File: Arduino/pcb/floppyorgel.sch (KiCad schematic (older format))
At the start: 25 parts, among them J1 Floppy-Bus, J2 Floppy-Bus, J3 FTDI, J4 Buck-Converter-5V, J5 MAX485 Socket, J6 Buck-Converter-12V, J7 IBM_PC_Floppy_IDC, J8 Power Select, J9 Floppy-Power, SW1 Bus Address Select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

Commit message: floppyorgel.sch: wiring shift registers
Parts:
- removed U3: 74LS166, SMD_Packages:SO-16-N, symbol floppyorgel-rescue:74LS166-74xx
- added R? (x4): 4K7, symbol Device:R
- added U?: 4021, symbol 4xxx_IEEE:4021
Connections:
- net labels added: DIRECTION, DRIVE_SELECT, STEP, TRK00, nLATCH
- wire segments 146 -> 162
- no-connect marks 15 -> 23
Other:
- moved on the sheet: C?, J7, R?, SW1, SW2, U1, Y1

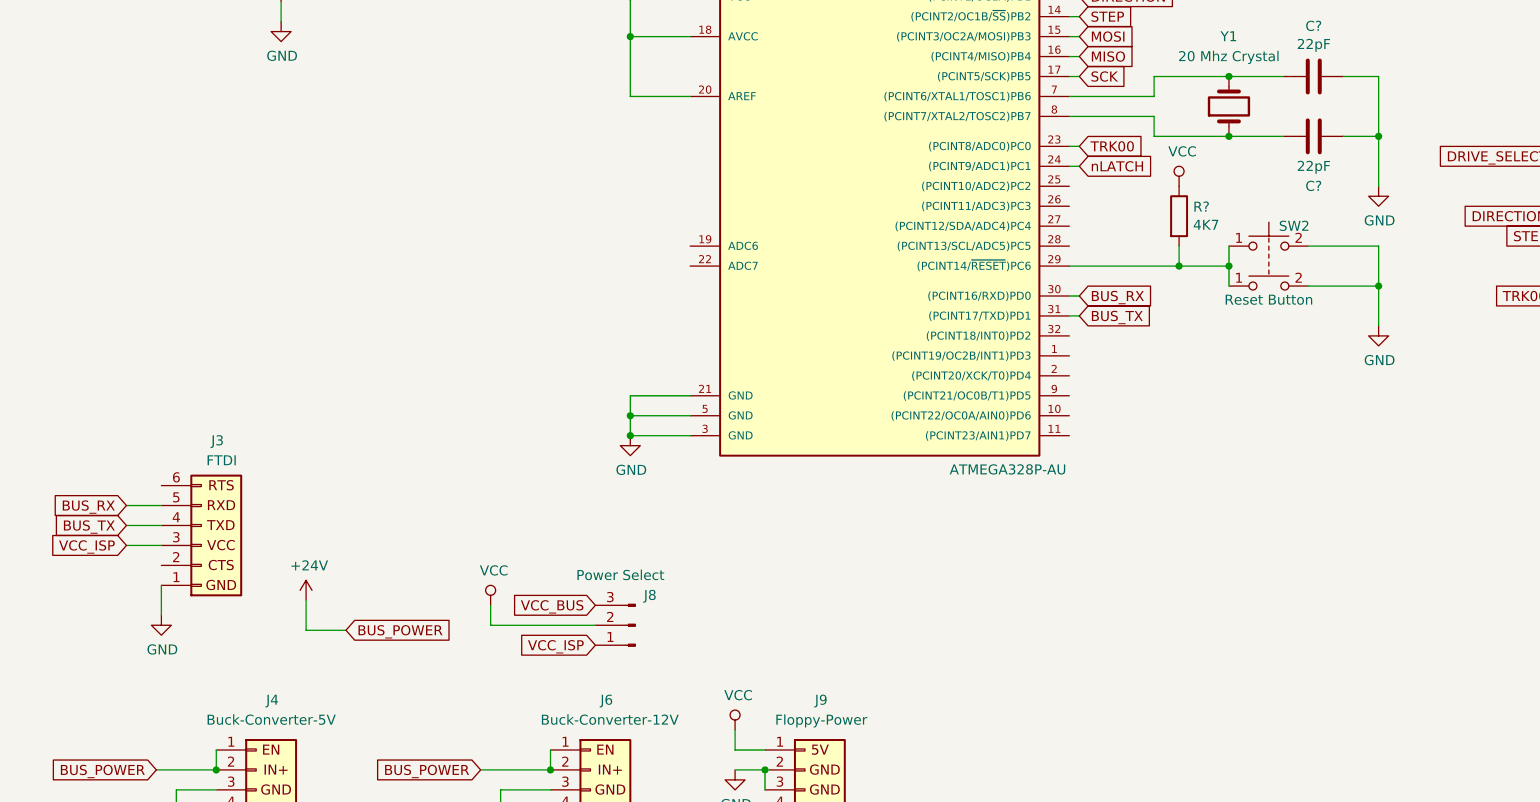
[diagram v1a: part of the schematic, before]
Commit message: floppyorgel.sch: wiring reset circuit
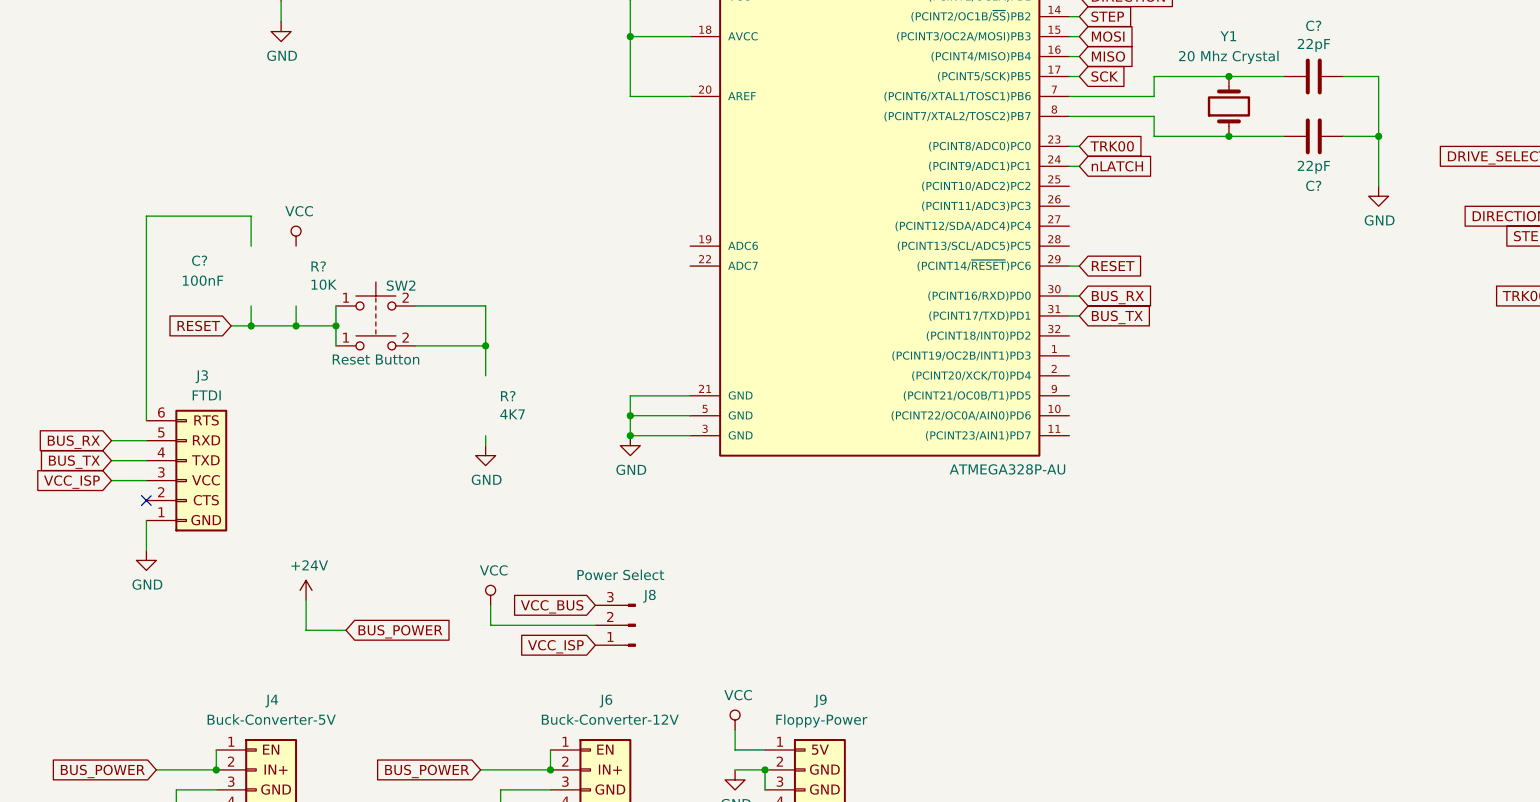
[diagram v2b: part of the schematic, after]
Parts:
- added C?: 100nF, symbol Device:C
- added R?: 4K7, symbol Device:R
- R?: value 4K7 -> 10K
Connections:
- net labels added: RESET
- wire segments 162 -> 169
- no-connect marks 23 -> 24
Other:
- moved on the sheet: J3, SW2
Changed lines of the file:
@@
 Sheet 1 1
 Title "Floppy Orgel"
-Date "2018-06-28"
+Date "2019-04-22"
 Rev "0"
 Comp "coon@c-base.org"
@@
 L floppyorgel-rescue:SW_Push_Dual-RESCUE-floppyorgel SW2
 U 1 1 5B36C9BB
-P 6825 4275
-F 0 "SW2" H 6875 4375 50  0000 L CNN
-F 1 "Reset Button" H 6825 4005 50  0000 C CNN
-F 2 "Buttons_Switches_THT:SW_PUSH_6mm" H 6825 4475 50  0001 C CNN
-F 3 "" H 6825 4475 50  0001 C CNN
-	1    6825 4275
+P 2350 4575
+F 0 "SW2" H 2400 4675 50  0000 L CNN
+F 1 "Reset Button" H 2350 4305 50  0000 C CNN
+F 2 "Buttons_Switches_THT:SW_PUSH_6mm" H 2350 4775 50  0001 C CNN
+F 3 "" H 2350 4775 50  0001 C CNN
+	1    2350 4575
 	1    0    0    -1
 $EndComp
@@
 L ftdi:FTDI J3
 U 1 1 5C74FB67
-P 1475 5775
-F 0 "J3" H 1525 5250 50  0000 L CNN
-F 1 "FTDI" H 1500 5350 50  0000 L CNN
-F 2 "Connector_PinHeader_2.54mm:PinHeader_1x06_P2.54mm_Vertical" H 1475 5775 50  0001 C CNN
-F 3 "" H 1475 5775 50  0001 C CNN
-	1    1475 5775
+P 1400 5450
+F 0 "J3" H 1450 4925 50  0000 L CNN
+F 1 "FTDI" H 1425 5025 50  0000 L CNN
+F 2 "Connector_PinHeader_2.54mm:PinHeader_1x06_P2.54mm_Vertical" H 1400 5450 50  0001 C CNN
+F 3 "" H 1400 5450 50  0001 C CNN
+	1    1400 5450
 	1    0    0    1
 $EndComp
@@
 $EndComp
 Wire Wire Line
-	6625 4375 6625 4275
-Wire Wire Line
-	6625 4475 6625 4375
-Connection ~ 6625 4375
+	2150 4675 2150 4575
+Wire Wire Line
+	2150 4775 2150 4675
+Connection ~ 2150 4675
 $Comp
 L power:GND #PWR?
 U 1 1 5CBED317
-P 7375 4675
-F 0 "#PWR?" H 7375 4425 50  0001 C CNN
-F 1 "GND" H 7380 4502 50  0000 C CNN
-F 2 "" H 7375 4675 50  0001 C CNN
-F 3 "" H 7375 4675 50  0001 C CNN
-	1    7375 4675
+P 2900 5275
+F 0 "#PWR?" H 2900 5025 50  0001 C CNN
+F 1 "GND" H 2905 5102 50  0000 C CNN
+F 2 "" H 2900 5275 50  0001 C CNN
+F 3 "" H 2900 5275 50  0001 C CNN
+	1    2900 5275
 	1    0    0    -1
 $EndComp
 $Comp
 L Device:R R?
-U 1 1 5CBEE8A7
-P 6375 4125
-F 0 "R?" H 6445 4171 50  0000 L CNN
-F 1 "4K7" H 6445 4080 50  0000 L CNN
-F 2 "" V 6305 4125 50  0001 C CNN
-F 3 "~" H 6375 4125 50  0001 C CNN
-	1    6375 4125
+U 0 0 5CBEE8A7
+P 1950 4425
+F 0 "R?" H 2020 4471 50  0000 L CNN
+F 1 "10K" H 2020 4380 50  0000 L CNN
+F 2 "" V 1880 4425 50  0001 C CNN
+F 3 "~" H 1950 4425 50  0001 C CNN
+	0    1950 4425
 	1    0    0    -1
 $EndComp
@@
 L power:VCC #PWR?
 U 1 1 5CBEF211
-P 6375 3975
-F 0 "#PWR?" H 6375 3825 50  0001 C CNN
-F 1 "VCC" H 6392 4148 50  0000 C CNN
-F 2 "" H 6375 3975 50  0001 C CNN
-F 3 "" H 6375 3975 50  0001 C CNN
-	1    6375 3975
+P 1950 4275
+F 0 "#PWR?" H 1950 4125 50  0001 C CNN
+F 1 "VCC" H 1967 4448 50  0000 C CNN
+F 2 "" H 1950 4275 50  0001 C CNN
+F 3 "" H 1950 4275 50  0001 C CNN
+	1    1950 4275
 	1    0    0    -1
 $EndComp
@@
 MISO
 Wire Wire Line
-	5825 4375 6375 4375
-Wire Wire Line
-	6375 4275 6375 4375
-Connection ~ 6375 4375
-Wire Wire Line
-	6375 4375 6625 4375
-Wire Wire Line
-	7375 4275 7375 4475
-Connection ~ 7375 4475
-Wire Wire Line
-	7375 4475 7375 4675
-Wire Wire Line
-	7025 4275 7375 4275
-Wire Wire Line
-	7025 4475 7375 4475
+	2900 4575 2900 4775
+Wire Wire Line
+	2550 4575 2900 4575
+Wire Wire Line
+	2550 4775 2900 4775
 $Comp
 L power:VCC #PWR?
@@
 L power:GND #PWR?
 U 1 1 5CBEBC38
-P 1275 6125
-F 0 "#PWR?" H 1275 5875 50  0001 C CNN
-F 1 "GND" H 1280 5952 50  0000 C CNN
-F 2 "" H 1275 6125 50  0001 C CNN
-F 3 "" H 1275 6125 50  0001 C CNN
-	1    1275 6125
-	1    0    0    -1
-$EndComp
-Wire Wire Line
-	1275 5975 1275 6125
+P 1200 5800
+F 0 "#PWR?" H 1200 5550 50  0001 C CNN
+F 1 "GND" H 1205 5627 50  0000 C CNN
+F 2 "" H 1200 5800 50  0001 C CNN
+F 3 "" H 1200 5800 50  0001 C CNN
+	1    1200 5800
+	1    0    0    -1
+$EndComp
+Wire Wire Line
+	1200 5650 1200 5800
 Text GLabel 3450 6075 0    50   Input ~ 0
 VCC_BUS
 Text GLabel 3450 6275 0    50   Input ~ 0
 VCC_ISP
-Text GLabel 1100 5575 0    50   Input ~ 0
+Text GLabel 1025 5250 0    50   Input ~ 0
 BUS_RX
-Text GLabel 1100 5675 0    50   Input ~ 0
+Text GLabel 1025 5350 0    50   Input ~ 0
 BUS_TX
 Wire Wire Line
-	1100 5575 1275 5575
-Wire Wire Line
-	1100 5675 1275 5675
-Text GLabel 1100 5775 0    50   Input ~ 0
+	1025 5250 1200 5250
+Wire Wire Line
+	1025 5350 1200 5350
+Text GLabel 1025 5450 0    50   Input ~ 0
 VCC_ISP
 Wire Wire Line
-	1100 5775 1275 5775
+	1025 5450 1200 5450
 Text GLabel 1750 7400 2    50   Input ~ 0
 VCC_BUS
@@
 Wire Wire Line
 	4450 875  4450 1275
+NoConn ~ 1200 5550
+Text GLabel 5875 4375 2    50   Input ~ 0
+RESET
+Text GLabel 1625 4675 0    50   Input ~ 0
+RESET
+Wire Wire Line
+	5825 4375 5875 4375
+$Comp
+L Device:C C?
+U 0 0 5CC1EA5F
+P 1725 4425
+F 0 "C?" H 1425 4500 50  0000 L CNN
+F 1 "100nF" H 1375 4400 50  0000 L CNN
+F 2 "" H 1763 4275 50  0001 C CNN
+F 3 "~" H 1725 4425 50  0001 C CNN
+	0    1725 4425
+	1    0    0    -1
+$EndComp
+Wire Wire Line
+	1200 4125 1725 4125
+Wire Wire Line
+	1625 4675 1725 4675
+Wire Wire Line
+	1725 4275 1725 4125
+Wire Wire Line
+	1200 4125 1200 5150
+Wire Wire Line
+	1725 4575 1725 4675
+Connection ~ 1725 4675
+Wire Wire Line
+	1725 4675 1950 4675
+Wire Wire Line
+	1950 4575 1950 4675
+Connection ~ 1950 4675
+Wire Wire Line
+	1950 4675 2150 4675
+$Comp
+L Device:R R?
+U 0 0 5CC73FA1
+P 2900 5075
+F 0 "R?" H 2970 5121 50  0000 L CNN
+F 1 "4K7" H 2970 5030 50  0000 L CNN
+F 2 "" V 2830 5075 50  0001 C CNN
+F 3 "~" H 2900 5075 50  0001 C CNN
+	0    2900 5075
+	1    0    0    -1
+$EndComp
+Wire Wire Line
+	2900 4925 2900 4775
+Connection ~ 2900 4775
+Wire Wire Line
+	2900 5275 2900 5225
 $EndSCHEMATC
